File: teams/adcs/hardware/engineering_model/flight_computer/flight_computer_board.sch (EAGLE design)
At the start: 79 parts, among them U1 Value, U2 Value

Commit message: ADCS/FSW: Finish reorganizing MSP432 board
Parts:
- removed C14, C15: 10uF, DubSat1 Components:CAPACITOR0805
- removed JP1, JP10, JP2, JP3, JP4, JP5, JP6, JP7, JP8, JP9: M02PTH, SparkFun-Connectors:M02PTH
- added C32, C45, C48, C55: 0.01 μF, rcl:C-USC0805
- added C36, C46, C49, C56: 1 μF, rcl:C-USC0805
- added C44, C47, C51, C57: 4.7 μF, rcl:C-USC0805
- added J1: FEMALE 2x3, SparkFun-Connectors:CONN_03X2FEMALE
- added J2: (no value), SparkFun-Connectors:CONN_08X2
- added U4, U5, U6, U8: LINEAR_LDO_LT1761-X, DubSat1 Components:LINEAR_LDO_LT1761-X
- C1: value 100n -> 0.1uF; device DubSat1 Components:CAPACITOR0805 -> rcl:C-USC0805
- C10, C40, C41, C9: value 12.5p -> 13 pF; device DubSat1 Components:CAPACITOR0805 -> rcl:C-USC0805
- C11, C12, C42, C43: value 10p -> 13 pF; device DubSat1 Components:CAPACITOR0805 -> rcl:C-USC0805
- C13, C2: value 10uF -> 10 uF; device DubSat1 Components:CAPACITOR0805 -> rcl:C-USC0805
- C16: value 4.7n -> 4.7 nF; device SparkFun-Capacitors:CAP0805 -> rcl:C-USC0805
- C17, C26, C34, C38, C4, C7: value 4.7u -> 4.7 uF; device DubSat1 Components:CAPACITOR0805 -> rcl:C-USC0805
- C18, C22: value 0.22µF -> 0.22 uF; device DubSat1 Components:CAPACITOR0805 -> rcl:C-USC0805
- C19, C27: value 1u -> 0.1 uF; device DubSat1 Components:CAPACITOR0805 -> rcl:C-USC0805
- C20, C21, C23, C28: value .1u -> 0.1 uF; device DubSat1 Components:CAPACITOR0805 -> rcl:C-USC0805
- C24, C25: value 0.1 μF -> 0.1 uF
- C3, C33, C35, C37, C39, C5, C50, C6, C8: value 100n -> 0.1 uF; device DubSat1 Components:CAPACITOR0805 -> rcl:C-USC0805
- R1, R2: value (none) -> 330 ohm
- R10, R3, R7, R9: value 2.2KΩ -> 10 kohm
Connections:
- removed net 3.3V: C1.1, C15.1, C23.1, C24.1, C25.2, C27.1, C28.1, C34.1, C35.1, C37.1, C38.1, C39.1, C4.1, C5.1, C50.1, C6.1, C7.1, C8.1, R10.1, R9.1, SDO/SA1.VCC, U$10.3.3V@1, U$10.3.3V@2, U$17.CS, U$17.VDD, U$17.VDDIO, U$18.!SPI_CS, U$18.I2C/!SPI, U$18.VDD, U$18.VDDIO, U$6.ESTIMAT_3.3V@75, U$6.ESTIMAT_3.3V@76, U$8.3.3V@1, U$8.3.3V@2, U1B.AVCC1, U1B.AVCC2, U1B.DVCC1, U1B.DVCC2, U2B.AVCC1, U2B.AVCC2, U2B.DVCC1, U2B.DVCC2
- removed net 3.3V-ISO: C13.1, C19.1, C20.1, C21.1, R3.1, R7.1, U$15.!SPI_CS, U$15.I2C/!SPI, U$15.VDD, U$15.VDDIO, U$6.BDOT_3.3V@83, U$6.BDOT_3.3V@84, U$7.3.3V_CAN@1, U$7.3.3V_CAN@2, U$7.3.3V_MSP-ANALOG@1, U$7.3.3V_MSP@2, U$7.3.3V_MSP@3
- removed net 5V: C14.1, U$10.5V, U$6.ESTIMAT_5V@73, U$6.ESTIMAT_5V@74, U$8.5V
- removed net 5V-ISO: C2.1, U$6.BDOT_5V@81, U$6.BDOT_5V@82, U$7.5V_CAN
- removed net GND: C1.2, C10.2, C11.2, C12.2, C14.2, C15.2, C16.2, C23.2, C24.2, C25.1, C26.2, C27.2, C28.2, C3.2, C33.2, C34.2, C35.2, C37.2, C38.2, C39.2, C4.2, C40.2, C41.2, C42.2, C43.2, C5.2, C50.2, C6.2, C7.2, C8.2, C9.2, R1.2, R2.2, SDO/SA1.GND, U$10.GND, U$11.14, U$11.20, U$11.3, U$11.6, U$12.14, U$12.20, U$12.3, U$12.6, U$13.14, U$13.20, U$13.3, U$13.6, U$17.GND@1, U$17.GND@2, U$17.SCX, U$17.SDX, U$18.GND, U$18.SOC, U$3.14, U$3.20, U$3.3, U$3.6, U$6.ESTIMAT_GND@79, U$6.ESTIMAT_GND@80, U$8.GND, U1B.AVSS1, U1B.AVSS2, U1B.AVSS3, U1B.DVSS1, U1B.DVSS2, U1B.DVSS3, U2B.AVSS1, U2B.AVSS2, U2B.AVSS3, U2B.DVSS1, U2B.DVSS2, U2B.DVSS3
- removed net GND-ISO: C13.2, C17.2, C19.2, C2.2, C20.2, C21.2, U$14.GND@1, U$14.GND@2, U$15.GND, U$15.SOC, U$6.BDOT_GND@87, U$6.BDOT_GND@88, U$7.GND
- removed net I2C_SCL2: JP2.1, JP2.2, JP3.1, R10.2, U$11.5, U$13.5, U$17.SCL, U2A.P6.5_UCB1SOMI_UCB1SCL_C1.2
- removed net I2C_SDA2: JP1.1, JP1.2, JP4.1, JP4.2, R9.2, U$11.4, U$13.4, U$17.SDA, U$18.SDA/SPI_SDI, U2A.P6.4_UCB1SIMO_UCB1SDA_C1.3
- removed net N$16: JP5.1, U$15.SDA/SPI_SDI
- removed net N$18: JP6.2, U$15.SCL/SPI_SCK
- removed net N$22: JP10.2, U$15.DRDY
- removed net N$26: JP3.2, U$18.SCL/SPI_SCK
- removed net N$27: JP6.1, R7.2, U$7.P5.1_I2C-SCL-1
- removed net N$28: JP5.2, R3.2, U$7.P5.0_I2C-SDA-1
- removed net N$29: JP8.2, U2A.P4.6_A7
- removed net N$30: JP7.1, U2A.P4.5_A8
- removed net N$31: JP10.1, U$7.P1.7_GPIO/PWM
- removed net N$32: JP9.2, U2A.P4.7_A6
- removed net N$38: JP7.2, U$18.DRDY
- new net BDOT_3V3: C19.1, C20.1, C21.1, C45.1, C47.2, R3.2, R7.2, U$15.!SPI_CS, U$15.I2C/!SPI, U$15.VDD, U$15.VDDIO, U$7.3.3V_CAN@1, U$7.3.3V_CAN@2, U$7.3.3V_MSP-ANALOG@1, U$7.3.3V_MSP@2, U$7.3.3V_MSP@3, U5.OUT
- new net BDOT_5V: C55.1, C57.2, U$7.5V_CAN, U8.OUT
- new net BDOT_DRDY: J1.6, U$15.DRDY
- new net BDOT_DRDY_JP: J1.5, U$7.P1.7_GPIO/PWM
- new net BDOT_GND: C13.2, C17.2, C19.2, C20.2, C21.2, C46.1, C47.1, C56.1, C57.1, U$14.GND@1, U$14.GND@2, U$15.GND, U$15.SOC, U$6.BDOT_GND@87, U$6.BDOT_GND@88, U$7.GND, U5.GND, U8.GND
- new net BDOT_LDO_3V3_BYP: C45.2, U5.BYP
- new net BDOT_LDO_5V_BYP: C55.2, U8.BYP
- new net BDOT_SCL: J1.4, U$15.SCL/SPI_SCK
- new net BDOT_SCL_JP: J1.3, R3.1, U$7.P5.1_I2C-SCL-1
- new net BDOT_SDA: J1.2, U$15.SDA/SPI_SDI
- new net BDOT_SDA_JP: J1.1, R7.1, U$7.P5.0_I2C-SDA-1
- new net BDOT_VBAT: C13.1, C46.2, C56.2, U$6.BDOT_VBAT@85, U$6.BDOT_VBAT@86, U5.EN, U5.IN, U8.EN, U8.IN
- new net ESTIMAT_3V3: C1.1, C23.1, C24.1, C25.2, C27.1, C28.1, C32.1, C34.1, C35.1, C37.1, C38.1, C39.1, C4.1, C44.2, C5.1, C50.1, C6.1, C7.1, C8.1, R10.1, R9.1, SDO/SA1.VCC, U$10.3.3V@1, U$10.3.3V@2, U$17.CS, U$17.VDD, U$17.VDDIO, U$18.!SPI_CS, U$18.I2C/!SPI, U$18.VDD, U$18.VDDIO, U$8.3.3V@1, U$8.3.3V@2, U1B.AVCC1, U1B.AVCC2, U1B.DVCC1, U1B.DVCC2, U2B.AVCC1, U2B.AVCC2, U2B.DVCC1, U2B.DVCC2, U4.OUT
- new net ESTIMAT_5V: C48.1, C51.2, U$10.5V, U$8.5V, U6.OUT
- new net ESTIMAT_DRDY: J2.14, U$18.DRDY
- new net ESTIMAT_DRDY_JP: J2.13, U2A.P4.5_A8
- new net ESTIMAT_GND: C1.2, C10.2, C11.2, C12.2, C16.2, C2.2, C23.2, C24.2, C25.1, C26.2, C27.2, C28.2, C3.2, C33.2, C34.2, C35.2, C36.1, C37.2, C38.2, C39.2, C4.2, C40.2, C41.2, C42.2, C43.2, C44.1, C49.1, C5.2, C50.2, C51.1, C6.2, C7.2, C8.2, C9.2, R1.2, R2.2, SDO/SA1.GND, U$10.GND, U$11.14, U$11.20, U$11.3, U$11.6, U$12.14, U$12.20, U$12.3, U$12.6, U$13.14, U$13.20, U$13.3, U$13.6, U$17.GND@1, U$17.GND@2, U$17.SCX, U$17.SDX, U$18.GND, U$3.14, U$3.20, U$3.3, U$3.6, U$6.ESTIMAT_GND@79, U$6.ESTIMAT_GND@80, U$8.GND, U1B.AVSS1, U1B.AVSS2, U1B.AVSS3, U1B.DVSS1, U1B.DVSS2, U1B.DVSS3, U2B.AVSS1, U2B.AVSS2, U2B.AVSS3, U2B.DVSS1, U2B.DVSS2, U2B.DVSS3, U4.GND, U6.GND
- new net ESTIMAT_IMU_INT1_JP: U2A.P4.6_A7
- new net ESTIMAT_INU_INT2_JP: U2A.P4.7_A6
- new net ESTIMAT_LDO_3V3_BYP: C32.2, U4.BYP
- new net ESTIMAT_LDO_5V_BYP: C48.2, U6.BYP
- new net ESTIMAT_MAG_SCL_IMU: J2.5
- new net ESTIMAT_SCL_IMU: J2.6, U$11.5, U$13.5, U$17.SCL
- new net ESTIMAT_SCL_JP: R10.2, U2A.P6.5_UCB1SOMI_UCB1SCL_C1.2
- new net ESTIMAT_SCL_MAG: J2.2, U$18.SCL/SPI_SCK
- new net ESTIMAT_SCL_MAG_JP: J2.1
- new net ESTIMAT_SDA_IMU: J2.8, U$17.SDA
- new net ESTIMAT_SDA_IMU_JP: J2.7
- new net ESTIMAT_SDA_JP: R9.2, U2A.P6.4_UCB1SIMO_UCB1SDA_C1.3
- new net ESTIMAT_SDA_MAG: J2.4, U$11.4, U$13.4, U$18.SDA/SPI_SDI
- new net ESTIMAT_SDA_MAG_JP: J2.3
- new net ESTIMAT_SOC: J2.16, U$18.SOC
- new net ESTIMAT_SOC_JP: J2.15, U2A.P4.1_A12
- new net ESTIMAT_VBAT: C2.1, C36.2, C49.2, U$6.ESTIMAT_VBAT@77, U$6.ESTIMAT_VBAT@78, U4.EN, U4.IN, U6.EN, U6.IN
- new net IMU_INT1_JP: J2.9
- new net IMU_INT2_JP: J2.11
- net IMU_INT1: now also J2.10; no longer JP9.1
- net IMU_INT2: now also J2.12; no longer JP8.1
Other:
- note added: "BDOT magnetometer"
- note added: "BDOT magnetometer config jumper"
- note added: "Estimator IMU"
- note added: "Estimator Magnetometer"
- note added: "Estimator sensor config jumper"
- note added: "Power/Smoothing for U1"
- note added: "Power/Smoothing for U2"
- note added: "Voltage Converters and Smoothing Capacitors"
- note removed: "Net Assignment and input bypass capacitors"
- moved on the sheet: C1, C10, C11, C12, C13, C16, C17, C18, C19, C2, C20, C21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

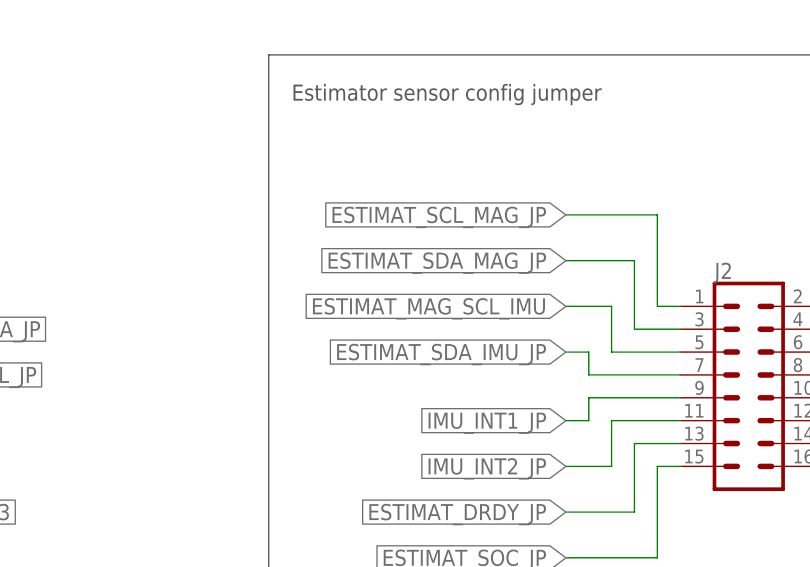
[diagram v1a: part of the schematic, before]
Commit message: ADCS/FSW: Route BDOT with new changes
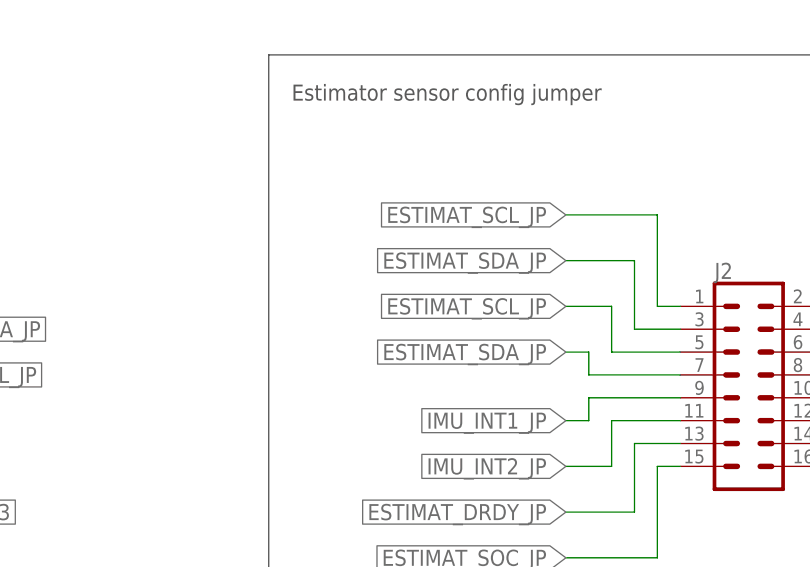
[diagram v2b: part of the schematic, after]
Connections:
- removed net ESTIMAT_MAG_SCL_IMU: J2.5
- removed net ESTIMAT_SCL_MAG_JP: J2.1
- removed net ESTIMAT_SDA_IMU_JP: J2.7
- removed net ESTIMAT_SDA_MAG_JP: J2.3
- net ESTIMAT_SCL_JP: now also J2.1, J2.5
- net ESTIMAT_SDA_JP: now also J2.3, J2.7
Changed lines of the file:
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@@
 <junction x="93.98" y="-134.62"/>
+</segment>
+<segment>
+<pinref part="J2" gate="G$1" pin="3"/>
+<wire x1="205.74" y1="-134.62" x2="200.66" y2="-134.62" width="0.1524" layer="91"/>
+<wire x1="200.66" y1="-134.62" x2="200.66" y2="-127" width="0.1524" layer="91"/>
+<wire x1="200.66" y1="-127" x2="193.04" y2="-127" width="0.1524" layer="91"/>
+<label x="193.04" y="-127" size="1.778" layer="95" rot="R180" xref="yes"/>
+</segment>
+<segment>
+<pinref part="J2" gate="G$1" pin="7"/>
+<wire x1="205.74" y1="-139.7" x2="195.58" y2="-139.7" width="0.1524" layer="91"/>
+<wire x1="195.58" y1="-139.7" x2="195.58" y2="-137.16" width="0.1524" layer="91"/>
+<wire x1="195.58" y1="-137.16" x2="193.04" y2="-137.16" width="0.1524" layer="91"/>
+<label x="193.04" y="-137.16" size="1.778" layer="95" rot="R180" xref="yes"/>
 </segment>
 </net>
@@
 <wire x1="101.6" y1="-142.24" x2="101.6" y2="-137.16" width="0.1524" layer="91"/>
 <junction x="101.6" y="-137.16"/>
+</segment>
+<segment>
+<pinref part="J2" gate="G$1" pin="1"/>
+<wire x1="205.74" y1="-132.08" x2="203.2" y2="-132.08" width="0.1524" layer="91"/>
+<wire x1="203.2" y1="-132.08" x2="203.2" y2="-121.92" width="0.1524" layer="91"/>
+<wire x1="203.2" y1="-121.92" x2="193.04" y2="-121.92" width="0.1524" layer="91"/>
+<label x="193.04" y="-121.92" size="1.778" layer="95" rot="R180" xref="yes"/>
+</segment>
+<segment>
+<pinref part="J2" gate="G$1" pin="5"/>
+<wire x1="205.74" y1="-137.16" x2="198.12" y2="-137.16" width="0.1524" layer="91"/>
+<wire x1="198.12" y1="-137.16" x2="198.12" y2="-132.08" width="0.1524" layer="91"/>
+<wire x1="198.12" y1="-132.08" x2="193.04" y2="-132.08" width="0.1524" layer="91"/>
+<label x="193.04" y="-132.08" size="1.778" layer="95" rot="R180" xref="yes"/>
 </segment>
 </net>
@@
 </segment>
 </net>
-<net name="ESTIMAT_SDA_IMU_JP" class="0">
-<segment>
-<pinref part="J2" gate="G$1" pin="7"/>
-<wire x1="205.74" y1="-139.7" x2="195.58" y2="-139.7" width="0.1524" layer="91"/>
-<wire x1="195.58" y1="-139.7" x2="195.58" y2="-137.16" width="0.1524" layer="91"/>
-<wire x1="195.58" y1="-137.16" x2="193.04" y2="-137.16" width="0.1524" layer="91"/>
-<label x="193.04" y="-137.16" size="1.778" layer="95" rot="R180" xref="yes"/>
-</segment>
-</net>
 <net name="IMU_INT1_JP" class="0">
 <segment>
@@
 </segment>
 </net>
-<net name="ESTIMAT_MAG_SCL_IMU" class="0">
-<segment>
-<pinref part="J2" gate="G$1" pin="5"/>
-<wire x1="205.74" y1="-137.16" x2="198.12" y2="-137.16" width="0.1524" layer="91"/>
-<wire x1="198.12" y1="-137.16" x2="198.12" y2="-132.08" width="0.1524" layer="91"/>
-<wire x1="198.12" y1="-132.08" x2="193.04" y2="-132.08" width="0.1524" layer="91"/>
-<label x="193.04" y="-132.08" size="1.778" layer="95" rot="R180" xref="yes"/>
-</segment>
-</net>
-<net name="ESTIMAT_SDA_MAG_JP" class="0">
-<segment>
-<pinref part="J2" gate="G$1" pin="3"/>
-<wire x1="205.74" y1="-134.62" x2="200.66" y2="-134.62" width="0.1524" layer="91"/>
-<wire x1="200.66" y1="-134.62" x2="200.66" y2="-127" width="0.1524" layer="91"/>
-<wire x1="200.66" y1="-127" x2="193.04" y2="-127" width="0.1524" layer="91"/>
-<label x="193.04" y="-127" size="1.778" layer="95" rot="R180" xref="yes"/>
-</segment>
-</net>
-<net name="ESTIMAT_SCL_MAG_JP" class="0">
-<segment>
-<pinref part="J2" gate="G$1" pin="1"/>
-<wire x1="205.74" y1="-132.08" x2="203.2" y2="-132.08" width="0.1524" layer="91"/>
-<wire x1="203.2" y1="-132.08" x2="203.2" y2="-121.92" width="0.1524" layer="91"/>
-<wire x1="203.2" y1="-121.92" x2="193.04" y2="-121.92" width="0.1524" layer="91"/>
-<label x="193.04" y="-121.92" size="1.778" layer="95" rot="R180" xref="yes"/>
-</segment>
-</net>

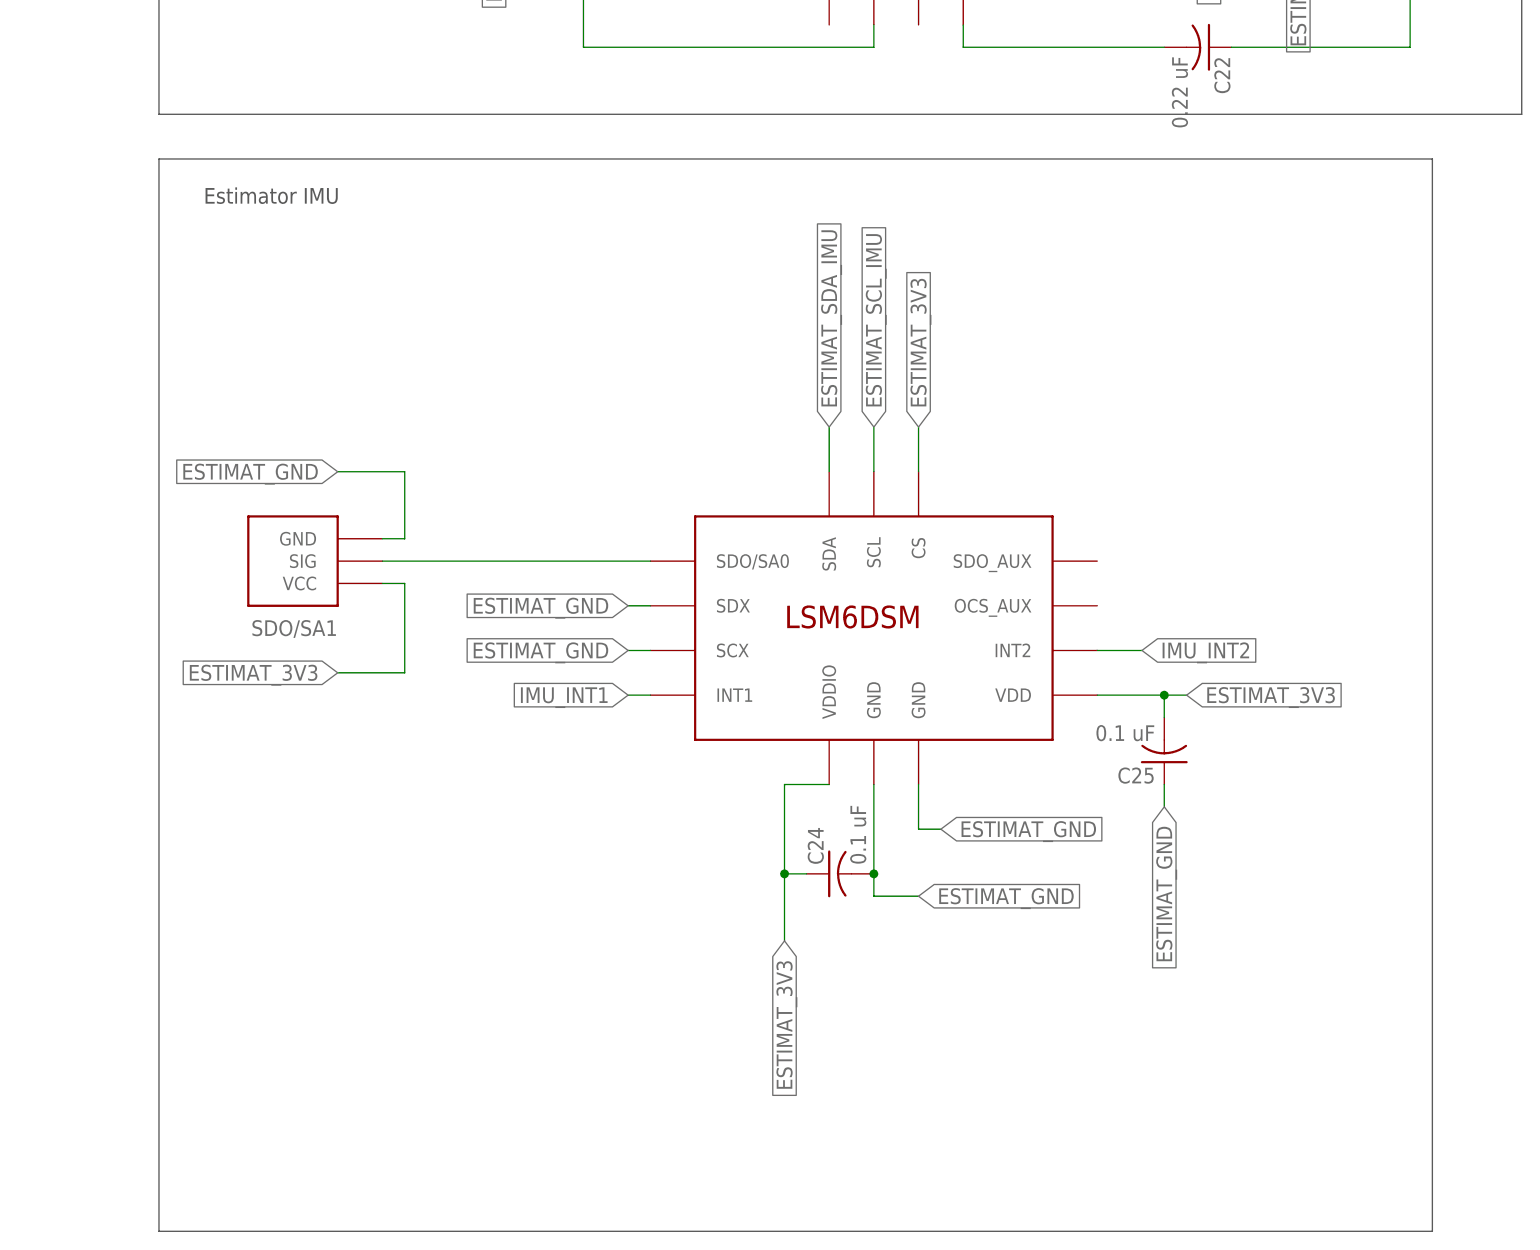
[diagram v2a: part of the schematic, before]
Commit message: ADCS/FSW: Add LDOs to the FSW board
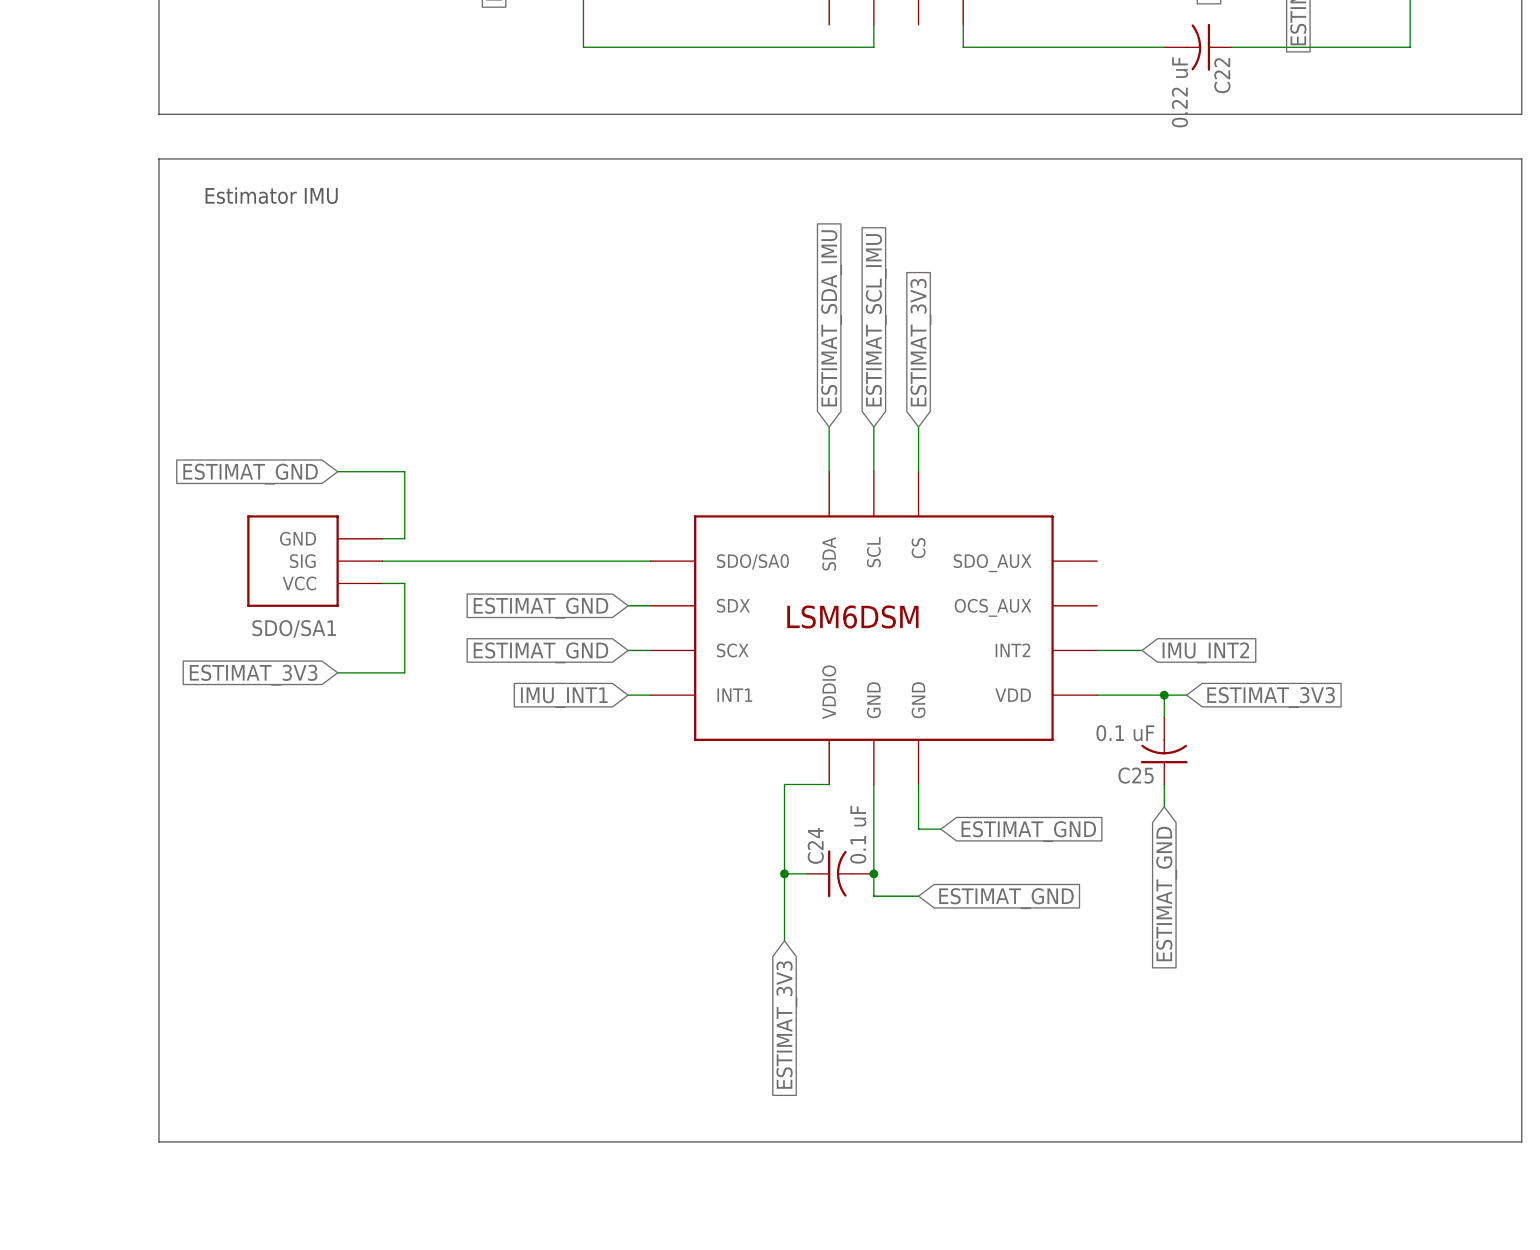
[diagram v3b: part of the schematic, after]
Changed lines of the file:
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@@
 <wire x1="-233.68" y1="-63.5" x2="-106.68" y2="-63.5" width="0.1524" layer="97"/>
 <wire x1="-106.68" y1="-63.5" x2="-106.68" y2="38.1" width="0.1524" layer="97"/>
-<wire x1="289.56" y1="-144.78" x2="434.34" y2="-144.78" width="0.1524" layer="97"/>
-<wire x1="434.34" y1="-144.78" x2="434.34" y2="-266.7" width="0.1524" layer="97"/>
-<wire x1="434.34" y1="-266.7" x2="289.56" y2="-266.7" width="0.1524" layer="97"/>
-<wire x1="289.56" y1="-266.7" x2="289.56" y2="-144.78" width="0.1524" layer="97"/>
+<wire x1="289.56" y1="-144.78" x2="444.5" y2="-144.78" width="0.1524" layer="97"/>
+<wire x1="444.5" y1="-144.78" x2="444.5" y2="-256.54" width="0.1524" layer="97"/>
+<wire x1="444.5" y1="-256.54" x2="289.56" y2="-256.54" width="0.1524" layer="97"/>
+<wire x1="289.56" y1="-256.54" x2="289.56" y2="-144.78" width="0.1524" layer="97"/>
 <text x="294.64" y="-149.86" size="1.778" layer="97">Estimator IMU</text>
 <text x="294.64" y="-22.86" size="1.778" layer="97">Estimator Magnetometer</text>
